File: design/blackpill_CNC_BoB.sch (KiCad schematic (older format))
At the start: 204 parts, among them J13 VMOT, J14 Spindle/Coolant, J19 AuxEncIn, J20 Power out, J23 Reset, U10 74LVC2G17, U2 TLP290-4, U3 TLP290-4, U8 TLP290-4

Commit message: power supply
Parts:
- added C?: 1000u, symbol Device:CP
- added C? (x4): 100nF, symbol Device:C
- added C? (x2): 10u, symbol Device:CP
- added D? (x2): LED, symbol Device:LED
- added R? (x2): 470, symbol Device:R
- added U?: LD1117S33TR_SOT223, Package_TO_SOT_SMD:SOT-223-3_TabPin2, symbol Regulator_Linear:LD1117S33TR_SOT223
- added U?: LD1117S50TR_SOT223, Package_TO_SOT_SMD:SOT-223-3_TabPin2, symbol Regulator_Linear:LD1117S50TR_SOT223
- R?: value 2k -> 1k5
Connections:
- net +12V: now also R?.2, C?.1, C?.1, C?.1, U?.3 (VI), U?.3 (VI)
- net +3V3: now also C?.1, C?.1, R?.2, U?.2 (VO)
- net +5V: now also C?.1, C?.1, R?.2, U?.2 (VO)
- net AuxO1L: no longer R?.2
- net GND: now also C?.2, C?.2, C?.2, C?.2, C?.2, C?.2, C?.2, D?.1 (K), D?.1 (K), U?.1 (GND), U?.1 (GND)
- new net: D?.2 (A), R?.1 (x2)
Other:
- moved on the sheet: D?

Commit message: fine tuning...
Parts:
- removed C1, C2, C3, C4: 100u, symbol Device:CP
- removed C? (x2): 100nF, symbol Device:C
- removed C?: 10u, symbol Device:CP
- removed D?: LED, symbol Device:LED
- removed J13: VMOT, symbol Connector_Generic:Conn_01x02
- removed J20: Power out, symbol Connector_Generic:Conn_02x02_Odd_Even
- removed R?: 470, symbol Device:R
- removed U?: LD1117S33TR_SOT223, Package_TO_SOT_SMD:SOT-223-3_TabPin2, symbol Regulator_Linear:LD1117S33TR_SOT223
- added C? (x3): 100nF, symbol Device:C
- added J?: 12V Power in, symbol Connector:Screw_Terminal_01x02
- added J?: 5V Power out, symbol Connector:Screw_Terminal_01x02
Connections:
- net GNDS is gone; now on net GND: J?.1 (Pin_1), J?.1 (Pin_1), J?.1 (Pin_1), J?.1 (Pin_1), J?.1 (Pin_1), J?.1 (Pin_1), J?.1 (Pin_1), J?.1 (Pin_1), J?.1 (Pin_1), U2.11, U2.13, U2.15, U2.9, U3.11, U3.13, U3.15, U3.9, U8.11, U8.9
- net VCC is gone; now on net +3V3: U10.5 (VCC), U10.5 (VCC)
- net +12V: now also J?.2 (Pin_2)
- net +3V3: now also C?.1, C?.2, C?.2
- net +5V: now also J?.2 (Pin_2)
- net GND: now also C?.1, C?.1, C?.2, J?.1 (Pin_1), J?.1 (Pin_1)
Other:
- moved on the sheet: C?, D?, J?, JP?, R?, RV?, U?, U?A, U?B, U?C

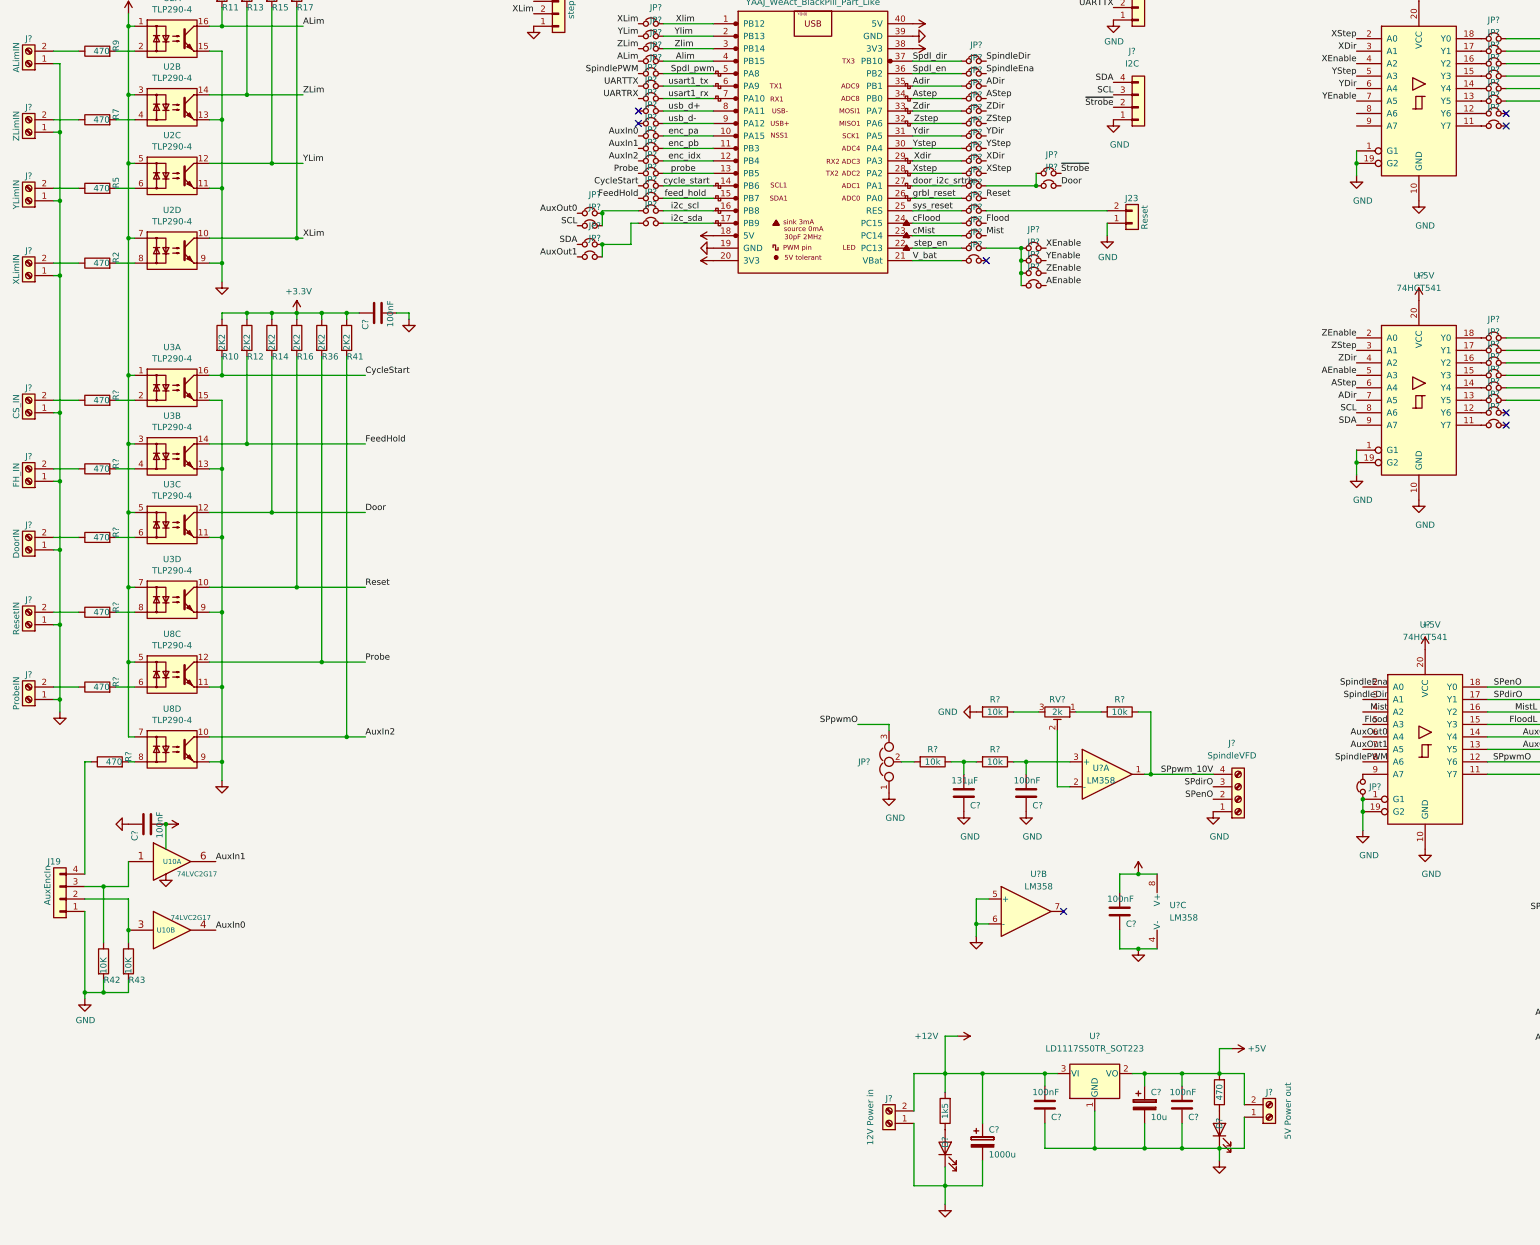
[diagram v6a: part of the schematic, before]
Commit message: analog input buffer
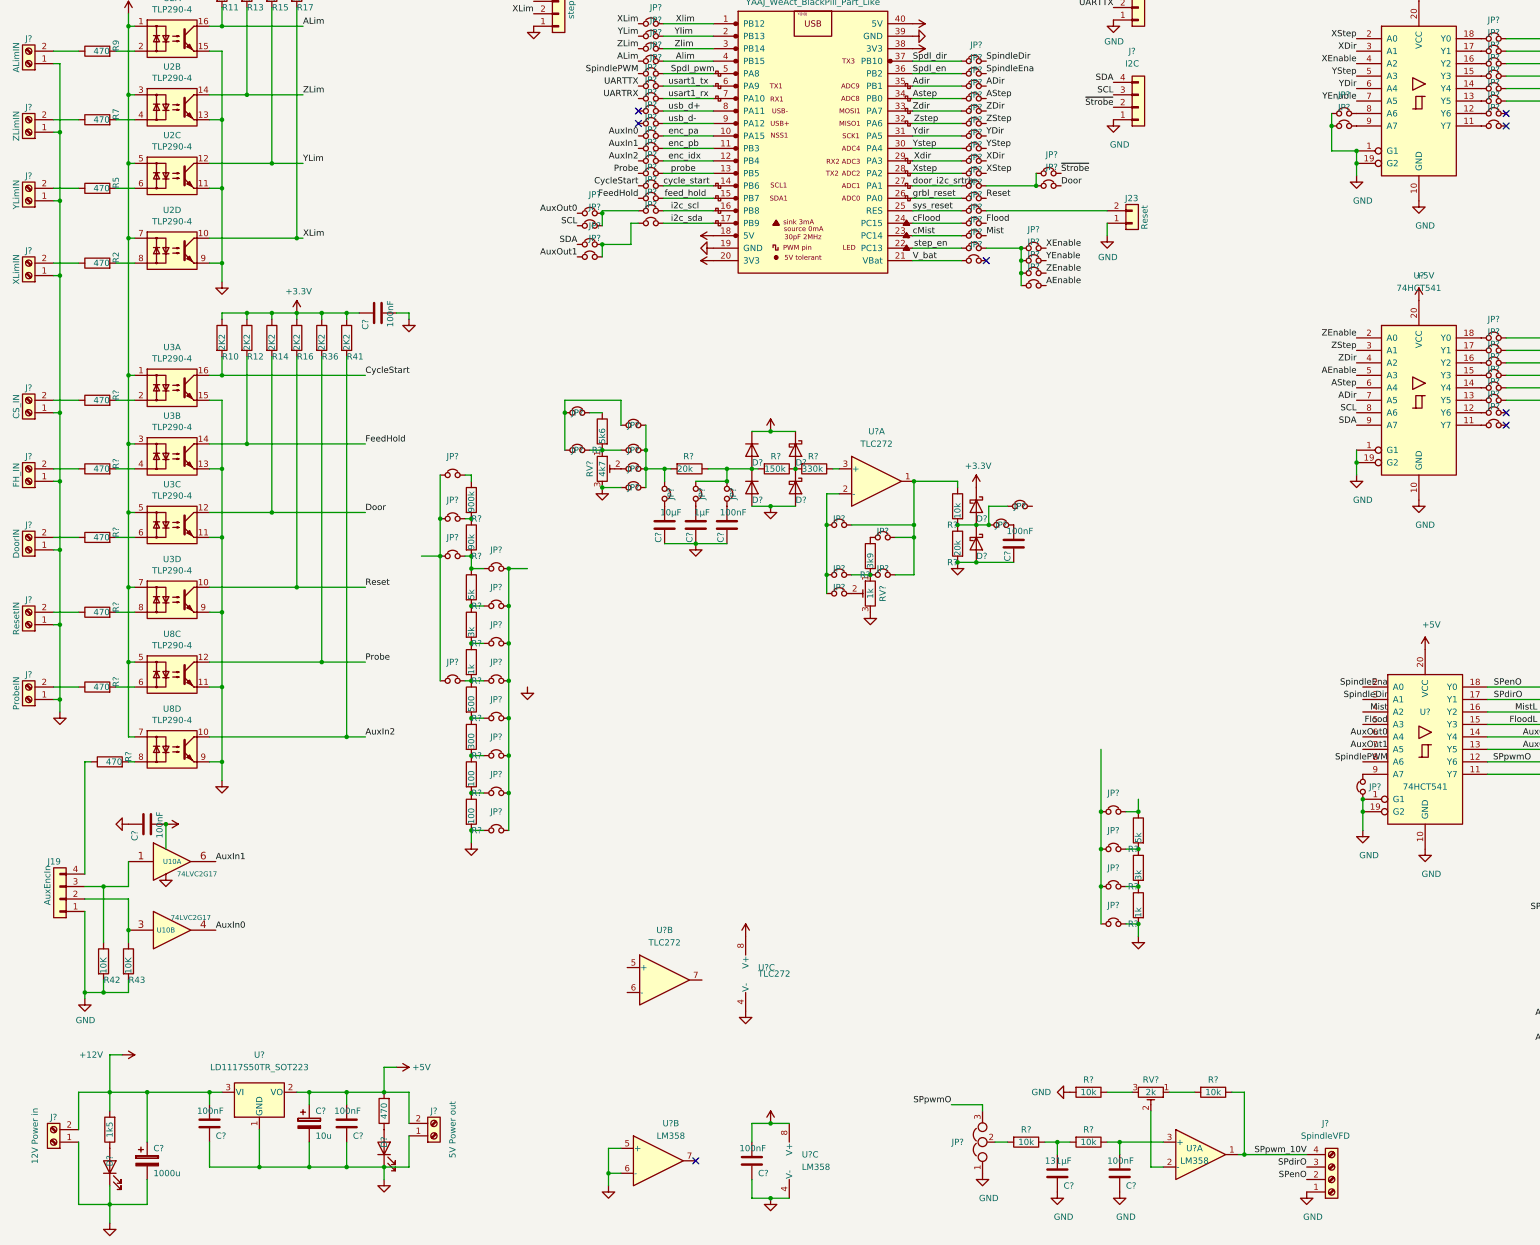
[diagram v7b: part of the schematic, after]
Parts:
- added C? (x2): 100nF, symbol Device:C
- added C?: 1µF, symbol Device:C
- added C?: 10µF, symbol Device:C
- added D? (x2): D, symbol Device:D
- added D? (x4): D_Schottky, symbol Device:D_Schottky
- added JP? (x34): Jumper_NC_Small, symbol Device:Jumper_NC_Small
- added R? (x2): 20k, symbol Device:R
- added R?: 150k, symbol Device:R
- added R?: 10k, symbol Device:R
- added R?: 330k, symbol Device:R
- added R? (x2): 100, symbol Device:R
- added R? (x2): 1k, symbol Device:R
- added R? (x2): 3k, symbol Device:R
- added R? (x2): 5k, symbol Device:R
- added R?: 90k, symbol Device:R
- added R?: 900k, symbol Device:R
- added R?: 300, symbol Device:R
- added R?: 500, symbol Device:R
- added R?: 5k6, symbol Device:R
- added R?: 3k9, symbol Device:R
- added RV?: 4k7, symbol Device:R_POT_TRIM
- added RV?: 1k, symbol Device:R_POT_TRIM
- added U? (x3): TLC272, symbol Amplifier_Operational:TLC272
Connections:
- net +3V3: now also D?.1 (K)
- net +5V: now also D?.1 (K), D?.1 (K), U?.8 (V+)
- net GND: now also C?.2, C?.2, C?.2, C?.2, D?.2 (A), D?.2 (A), D?.2 (A), JP?.1, JP?.1, JP?.1, JP?.1, JP?.2, R?.2, R?.2, R?.2, RV?.3, RV?.3, U?.4 (V-)
- net at U?.8 (A6): now also JP?.2
- net at U?.9 (A7): now also JP?.2
- new net: D?.1 (K), D?.2 (A), JP?.2, JP?.2, R?.1, R?.2 (x2)
- new net: JP?.1, JP?.1, JP?.1, JP?.1, JP?.2, R?.2
- new net: D?.1 (K), D?.2 (A), R?.1, R?.2
- new net: JP?.1, RV?.2
- new net: JP?.2, JP?.2, JP?.2, U?.2 (-)
- new net: JP?.1, JP?.1, JP?.1, R?.1, U?.1
- new net: C?.1, JP?.1 (x4)
- new net: R?.1, U?.3 (+)
- new net: JP?.1, R?.1, R?.2 (x7)
- new net: JP?.1, JP?.2, R?.1, R?.2 (x2)
- new net: JP?.2, R?.1, R?.2
- new net: JP?.2, R?.1 (x2)
- new net: JP?.1, JP?.1, JP?.1, JP?.1
- new net: JP?.2, JP?.2, JP?.2, JP?.2, JP?.2, JP?.2, JP?.2, JP?.2
- new net: JP?.1, R?.1 (x2)
- new net: JP?.2, JP?.2, JP?.2, JP?.2
- new net: JP?.1, JP?.2, R?.2, RV?.1 (x2)
- new net: JP?.2, RV?.2
- new net: JP?.2, JP?.2, JP?.2
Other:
- moved on the sheet: C?, D?, J?, JP?, R?, RV?, U?, U?A, U?B, U?C

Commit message: redraft, before annotation reorder
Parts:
- removed JP? (x16): Jumper_NC_Small, symbol Device:Jumper_NC_Small
- removed R? (x2): 100, symbol Device:R
- removed R? (x2): 1k, symbol Device:R
- removed R? (x2): 3k, symbol Device:R
- removed R? (x2): 5k, symbol Device:R
- removed R?: 90k, symbol Device:R
- removed R?: 900k, symbol Device:R
- removed R?: 300, symbol Device:R
- removed R?: 500, symbol Device:R
- C?: value 100nF -> 10nF
